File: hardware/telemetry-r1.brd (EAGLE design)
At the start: 63.5 x 63.5 mm, 113 parts, among them IC1 COPERNICUSSMD, IC10 TPS70933, IC2 TPS70933, IC3 74HC137, IC4 STM32L073CZT6, IC5 TPS62160, IC6 HX1, IC7 LMP7702, IC8 ADXL345, IC9 HIH9131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

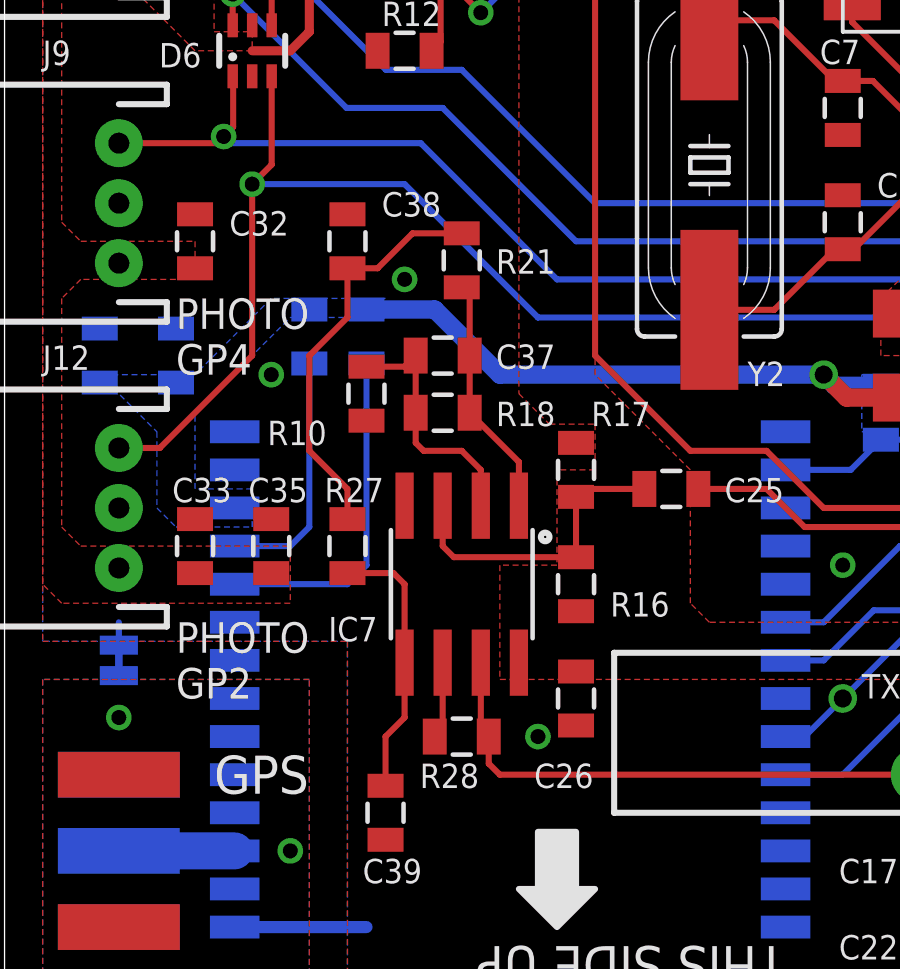
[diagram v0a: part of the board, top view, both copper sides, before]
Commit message: Update HX1 filter to match latest experimental results
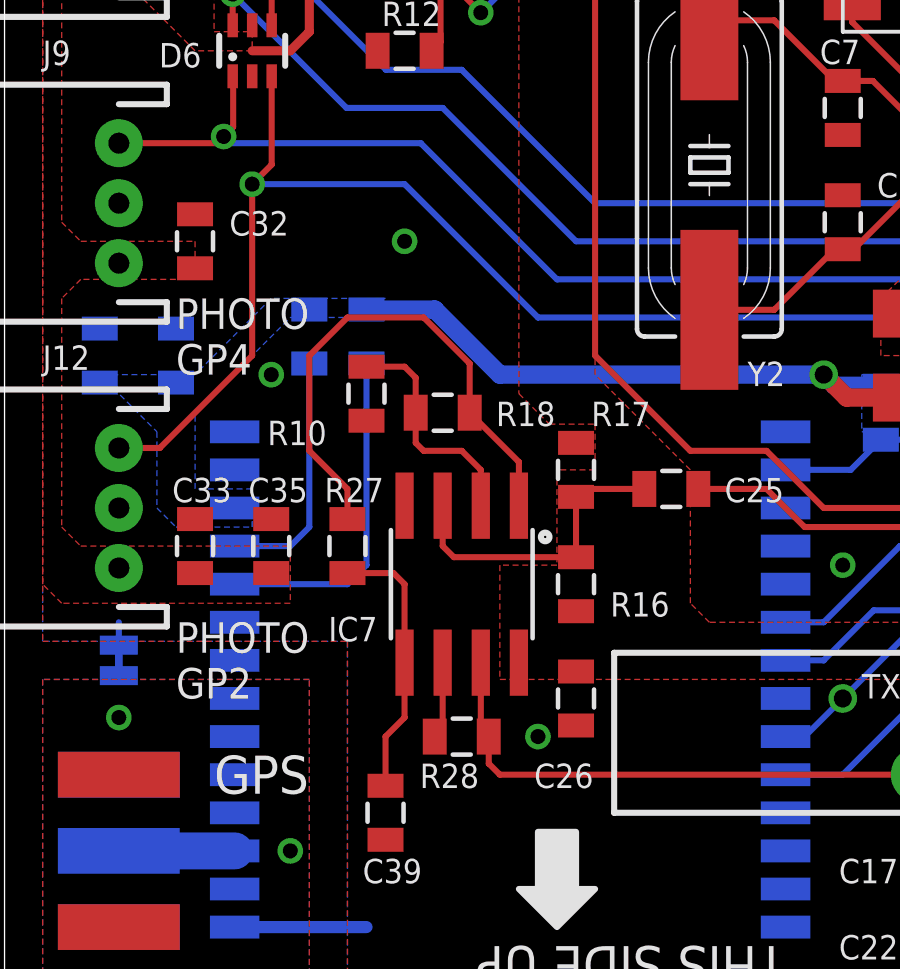
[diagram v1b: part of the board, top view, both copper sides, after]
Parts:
- removed C37: 100p, SparkFun-Passives:0805
- removed C38: 47n, SparkFun-Passives:0805
- removed R21: 680, SparkFun-Passives:0805
- R10: value 18K -> 470K
- R16: value 470K -> 820K
- R18: value 10K -> 680K
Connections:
- removed net LP3: C39.1, IC7.5, R27.2
- net A-: no longer C37.2
- net GND: no longer C38.2
- net LP1: now also R27.1; no longer C37.1, R21.1
- net LP2: now also C39.1, IC7.5, R27.2; no longer C38.1, R21.2, R27.1
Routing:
- net LP1: track 8.07 -> 17.9 mm
- net LP3: track 9.04 -> 0.00 mm
- net LP2: track 13.7 -> 9.04 mm
- net A-: track 8.44 -> 7.70 mm
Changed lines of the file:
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@@
 <attribute name="VALUE" x="40.513" y="15.621" size="0.6096" layer="27" rot="R270"/>
 </element>
-<element name="R16" library="SparkFun-Passives" package="0805" value="470K" x="19.05" y="15.24" smashed="yes" rot="R270">
+<element name="R16" library="SparkFun-Passives" package="0805" value="820K" x="19.05" y="15.24" smashed="yes" rot="R270">
 <attribute name="NAME" x="20.193" y="14.1605" size="0.8128" layer="25"/>
 <attribute name="VALUE" x="20.574" y="13.208" size="0.6096" layer="27"/>
@@
 <attribute name="VALUE" x="19.558" y="20.066" size="0.6096" layer="27" rot="R270"/>
 </element>
-<element name="R18" library="SparkFun-Passives" package="0805" value="10K" x="14.605" y="20.955" smashed="yes">
+<element name="R18" library="SparkFun-Passives" package="0805" value="680K" x="14.605" y="20.955" smashed="yes">
 <attribute name="NAME" x="16.383" y="20.5105" size="0.8128" layer="25"/>
 <attribute name="VALUE" x="16.764" y="21.463" size="0.6096" layer="27"/>
@@
 <element name="U$2" library="HAB" package="GARAGE" value="" x="29.21" y="41.91" rot="MR0"/>
 <element name="U$5" library="HAB" package="SWIFT" value="" x="27.305" y="52.705" rot="MR0"/>
-<element name="C37" library="SparkFun-Passives" package="0805" value="100p" x="14.605" y="22.86" smashed="yes" rot="R180">
-<attribute name="NAME" x="16.383" y="22.4155" size="0.8128" layer="25"/>
-<attribute name="VALUE" x="16.764" y="23.368" size="0.6096" layer="27"/>
-</element>
-<element name="R10" library="SparkFun-Passives" package="0805" value="18K" x="12.065" y="21.59" smashed="yes" rot="R90">
+<element name="R10" library="SparkFun-Passives" package="0805" value="470K" x="12.065" y="21.59" smashed="yes" rot="R90">
 <attribute name="NAME" x="8.763" y="19.8755" size="0.8128" layer="25"/>
 <attribute name="VALUE" x="9.779" y="20.828" size="0.6096" layer="27"/>
-</element>
-<element name="R21" library="SparkFun-Passives" package="0805" value="680" x="15.24" y="26.035" smashed="yes" rot="R90">
-<attribute name="NAME" x="16.383" y="25.5905" size="0.8128" layer="25"/>
-<attribute name="VALUE" x="16.129" y="26.543" size="0.6096" layer="27"/>
-</element>
-<element name="C38" library="SparkFun-Passives" package="0805" value="47n" x="11.43" y="26.67" smashed="yes" rot="R90">
-<attribute name="NAME" x="12.573" y="27.4955" size="0.8128" layer="25"/>
-<attribute name="VALUE" x="10.414" y="28.448" size="0.6096" layer="27"/>
 </element>
 <element name="R27" library="SparkFun-Passives" package="0805" value="330k" x="11.43" y="16.51" smashed="yes" rot="R270">
@@
 <contactref element="D10" pad="A"/>
 <contactref element="D4" pad="A"/>
-<contactref element="C38" pad="2"/>
 <contactref element="C39" pad="2"/>
 <contactref element="R10" pad="1"/>
 <contactref element="IC7" pad="4"/>
-<via x="13.335" y="25.4" extent="1-16" drill="0.5"/>
+<via x="13.335" y="26.67" extent="1-16" drill="0.5"/>
 </signal>
 <signal name="3.3V">
@@
 <signal name="A-">
 <contactref element="R10" pad="2"/>
-<contactref element="C37" pad="2"/>
 <contactref element="R18" pad="1"/>
-<wire x1="13.705" y1="20.955" x2="13.705" y2="22.86" width="0.2032" layer="1"/>
 <wire x1="12.065" y1="22.49" x2="13.335" y2="22.49" width="0.2032" layer="1"/>
-<wire x1="13.335" y1="22.49" x2="13.705" y2="22.86" width="0.2032" layer="1"/>
 <contactref element="IC7" pad="2"/>
 <wire x1="15.875" y1="17.8562" x2="15.875" y2="19.05" width="0.2032" layer="1"/>
@@
 <wire x1="13.705" y1="20.955" x2="13.705" y2="19.95" width="0.2032" layer="1"/>
 <wire x1="13.705" y1="19.95" x2="13.97" y2="19.685" width="0.2032" layer="1"/>
+<wire x1="13.705" y1="20.955" x2="13.705" y2="22.12" width="0.2032" layer="1"/>
+<wire x1="13.705" y1="22.12" x2="13.335" y2="22.49" width="0.2032" layer="1"/>
 </signal>
 <signal name="A+">
@@
 </signal>
 <signal name="LP1">
-<contactref element="R21" pad="1"/>
 <contactref element="IC7" pad="1"/>
 <contactref element="R18" pad="2"/>
-<contactref element="C37" pad="1"/>
 <wire x1="17.145" y1="17.8562" x2="17.145" y2="19.315" width="0.2032" layer="1"/>
 <wire x1="17.145" y1="19.315" x2="15.505" y2="20.955" width="0.2032" layer="1"/>
-<wire x1="15.505" y1="20.955" x2="15.505" y2="22.86" width="0.2032" layer="1"/>
-<wire x1="15.505" y1="22.86" x2="15.505" y2="24.87" width="0.2032" layer="1"/>
-<wire x1="15.505" y1="24.87" x2="15.24" y2="25.135" width="0.2032" layer="1"/>
-</signal>
-<signal name="LP2">
-<contactref element="C38" pad="1"/>
-<contactref element="R21" pad="2"/>
 <contactref element="R27" pad="1"/>
-<wire x1="11.43" y1="25.77" x2="12.435" y2="25.77" width="0.2032" layer="1"/>
-<wire x1="15.24" y1="26.935" x2="13.6" y2="26.935" width="0.2032" layer="1"/>
-<wire x1="13.6" y1="26.935" x2="12.435" y2="25.77" width="0.2032" layer="1"/>
 <wire x1="11.43" y1="17.41" x2="11.43" y2="18.415" width="0.2032" layer="1"/>
 <wire x1="11.43" y1="18.415" x2="10.16" y2="19.685" width="0.2032" layer="1"/>
 <wire x1="10.16" y1="19.685" x2="10.16" y2="22.86" width="0.2032" layer="1"/>
 <wire x1="10.16" y1="22.86" x2="11.43" y2="24.13" width="0.2032" layer="1"/>
-<wire x1="11.43" y1="25.77" x2="11.43" y2="24.13" width="0.2032" layer="1"/>
-</signal>
-<signal name="LP3">
-<contactref element="R27" pad="2"/>
-<contactref element="C39" pad="1"/>
+<wire x1="15.505" y1="20.955" x2="15.505" y2="22.595" width="0.2032" layer="1"/>
+<wire x1="15.505" y1="22.595" x2="13.97" y2="24.13" width="0.2032" layer="1"/>
+<wire x1="13.97" y1="24.13" x2="11.43" y2="24.13" width="0.2032" layer="1"/>
+</signal>
+<signal name="LP2">
 <contactref element="IC7" pad="5"/>
 <wire x1="13.335" y1="12.6238" x2="13.335" y2="10.795" width="0.2032" layer="1"/>
 <wire x1="13.335" y1="10.795" x2="12.7" y2="10.16" width="0.2032" layer="1"/>
-<wire x1="12.7" y1="10.16" x2="12.7" y2="8.52" width="0.2032" layer="1"/>
-<wire x1="11.43" y1="15.61" x2="12.965" y2="15.61" width="0.2032" layer="1"/>
 <wire x1="12.965" y1="15.61" x2="13.335" y2="15.24" width="0.2032" layer="1"/>
 <wire x1="13.335" y1="15.24" x2="13.335" y2="12.6238" width="0.2032" layer="1"/>
+<contactref element="R27" pad="2"/>
+<contactref element="C39" pad="1"/>
+<wire x1="12.965" y1="15.61" x2="11.43" y2="15.61" width="0.2032" layer="1"/>
+<wire x1="12.7" y1="8.52" x2="12.7" y2="10.16" width="0.2032" layer="1"/>
 </signal>
 <signal name="LP-">

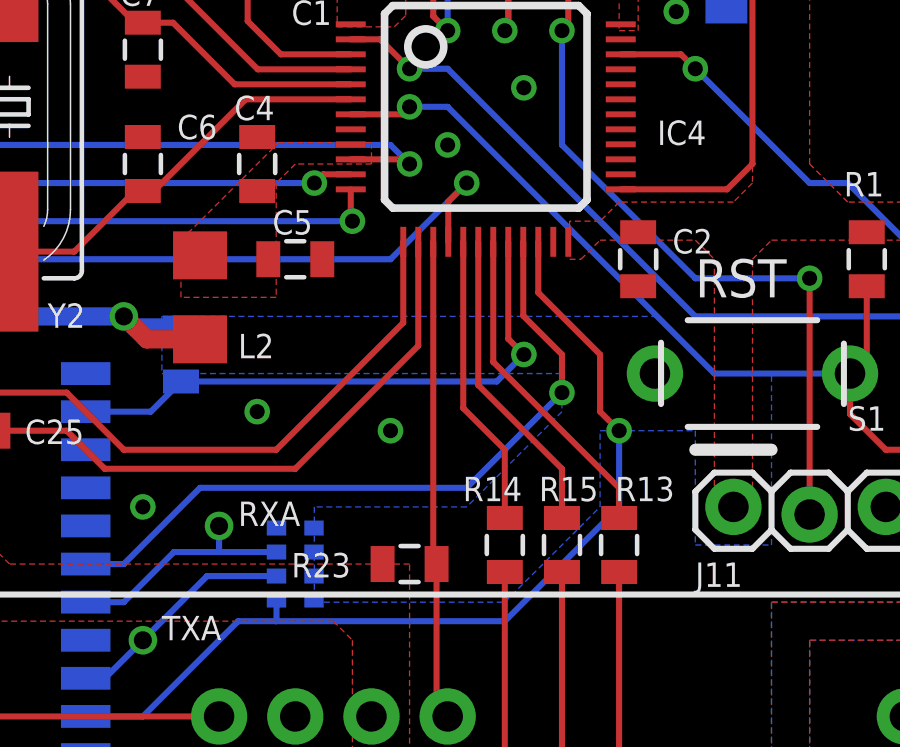
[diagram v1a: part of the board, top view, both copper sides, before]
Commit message: Swap HXEN pin to 5VT pin
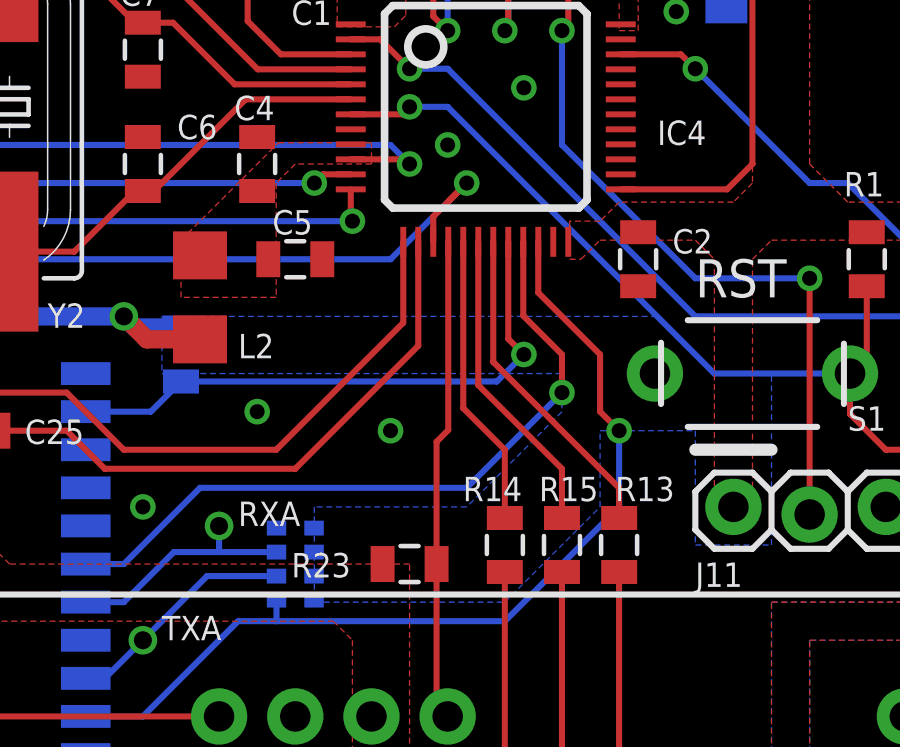
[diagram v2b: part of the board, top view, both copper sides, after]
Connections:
- net HXEN: now also IC4.16; no longer IC4.15
- net PHOTO_GP2: now also IC4.15; no longer IC4.16
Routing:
- net PHOTO_GP2: track 50.9 -> 52.0 mm
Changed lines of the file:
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@@
 <contactref element="IC6" pad="4"/>
 <contactref element="R23" pad="1"/>
-<contactref element="IC4" pad="15"/>
 <wire x1="37.73" y1="13.97" x2="37.73" y2="9.26" width="0.2032" layer="1"/>
 <wire x1="37.73" y1="9.26" x2="38.1" y2="8.89" width="0.2032" layer="1"/>
-<wire x1="37.62" y1="24.71" x2="37.62" y2="14.08" width="0.2032" layer="1"/>
 <wire x1="37.62" y1="14.08" x2="37.73" y2="13.97" width="0.2032" layer="1"/>
+<contactref element="IC4" pad="16"/>
+<wire x1="38.12" y1="24.71" x2="38.12" y2="18.435" width="0.2032" layer="1"/>
+<wire x1="37.73" y1="13.97" x2="37.73" y2="18.045" width="0.2032" layer="1"/>
+<wire x1="37.73" y1="18.045" x2="38.12" y2="18.435" width="0.2032" layer="1"/>
 </signal>
 <signal name="ADXL_SDO">
@@
 <contactref element="J12" pad="3"/>
 <contactref element="D6" pad="3"/>
-<contactref element="IC4" pad="16"/>
 <wire x1="8.905" y1="32.17" x2="8.905" y2="29.225" width="0.2032" layer="1"/>
 <wire x1="8.905" y1="29.225" x2="8.255" y2="28.575" width="0.2032" layer="1"/>
@@
 <wire x1="13.335" y1="28.575" x2="8.255" y2="28.575" width="0.2032" layer="16"/>
 <via x="8.255" y="28.575" extent="1-16" drill="0.5"/>
-<wire x1="38.12" y1="24.71" x2="38.12" y2="26.055" width="0.2032" layer="1"/>
 <wire x1="38.12" y1="26.055" x2="38.735" y2="26.67" width="0.2032" layer="1"/>
+<contactref element="IC4" pad="15"/>
+<wire x1="37.62" y1="24.71" x2="37.62" y2="25.555" width="0.2032" layer="1"/>
+<wire x1="37.62" y1="25.555" x2="38.735" y2="26.67" width="0.2032" layer="1"/>
 </signal>
 <signal name="USIN">

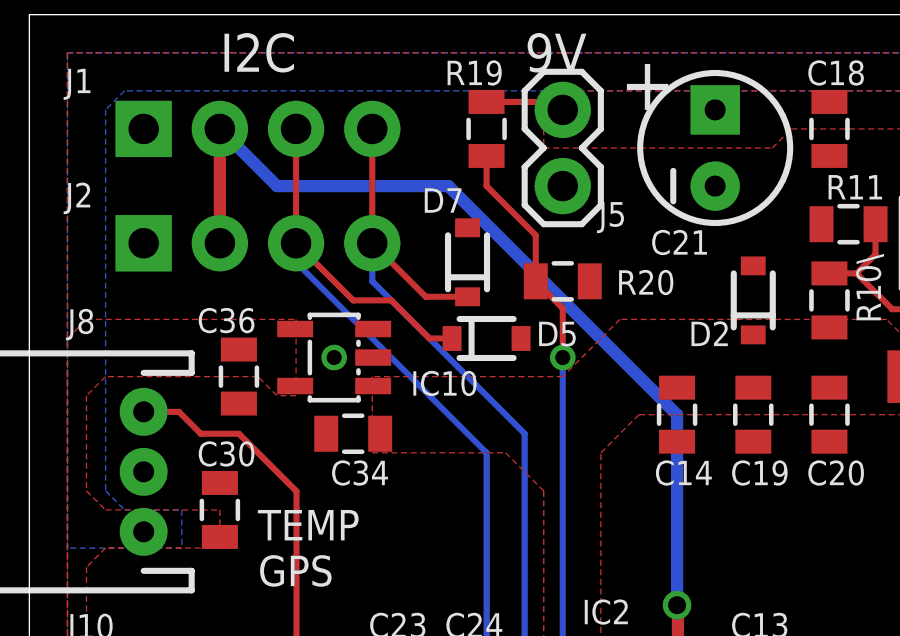
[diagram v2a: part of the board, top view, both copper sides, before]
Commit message: Fix I2C pull-up resistors in beta/regular boards; add Phoenix board and some datasheets
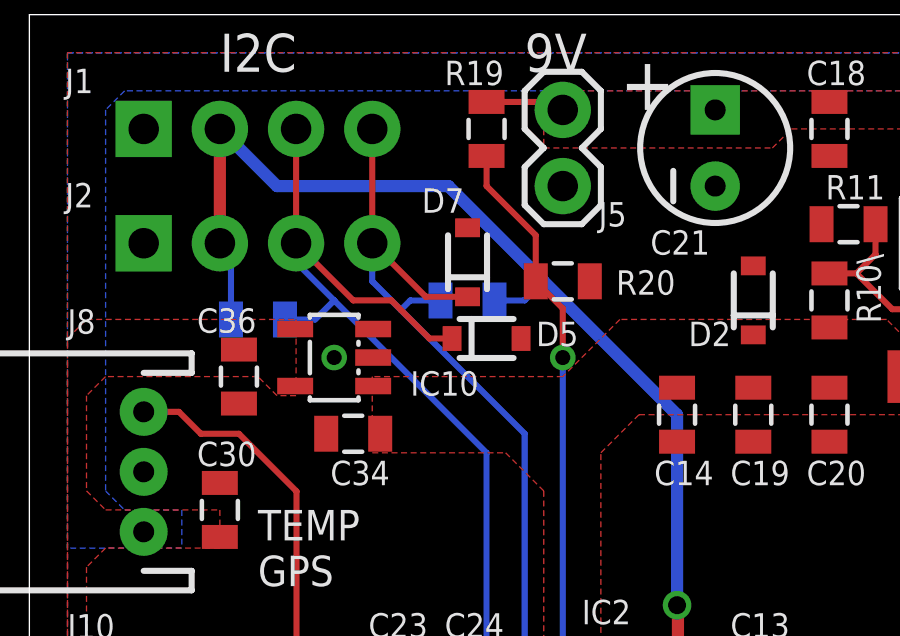
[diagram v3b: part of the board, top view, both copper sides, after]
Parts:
- added R21, R29: 4.7K, SparkFun-Passives:0805
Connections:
- net 3.3V: now also R21.1, R29.1
- net SCL: now also R21.2
- net SDA: now also R29.2
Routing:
- net 3.3V: track 86.8 -> 91.4 mm
- net SDA: track 63.2 -> 65.1 mm
- net SCL: track 54.3 -> 55.7 mm
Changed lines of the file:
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@@
 <attribute name="VALUE" x="14.859" y="7.493" size="0.6096" layer="27"/>
+</element>
+<element name="R21" library="SparkFun-Passives" package="0805" value="4.7K" x="14.605" y="53.975" smashed="yes" rot="MR0">
+<attribute name="NAME" x="15.367" y="54.8005" size="0.6096" layer="26" rot="MR0"/>
+<attribute name="VALUE" x="15.621" y="52.578" size="0.4064" layer="28" rot="MR0"/>
+</element>
+<element name="R29" library="SparkFun-Passives" package="0805" value="4.7K" x="7.62" y="53.34" smashed="yes" rot="MR180">
+<attribute name="NAME" x="6.858" y="52.5145" size="0.6096" layer="26" rot="MR180"/>
+<attribute name="VALUE" x="6.604" y="54.737" size="0.4064" layer="28" rot="MR180"/>
 </element>
 </elements>
@@
 <via x="21.59" y="43.815" extent="1-16" drill="0.6"/>
 <wire x1="21.59" y1="43.815" x2="21.59" y2="50.165" width="0.4064" layer="16"/>
-<wire x1="21.59" y1="50.165" x2="13.97" y2="57.785" width="0.4064" layer="16"/>
+<wire x1="21.59" y1="50.165" x2="17.145" y2="54.61" width="0.4064" layer="16"/>
+<wire x1="17.145" y1="54.61" x2="13.97" y2="57.785" width="0.4064" layer="16"/>
 <wire x1="13.97" y1="57.785" x2="8.255" y2="57.785" width="0.4064" layer="16"/>
 <wire x1="8.255" y1="57.785" x2="6.35" y2="59.69" width="0.4064" layer="16"/>
@@
 <vertex x="38.1" y="39.37"/>
 </polygon>
+<contactref element="R21" pad="1"/>
+<contactref element="R29" pad="1"/>
+<wire x1="15.505" y1="53.975" x2="16.51" y2="53.975" width="0.2032" layer="16"/>
+<wire x1="16.51" y1="53.975" x2="17.145" y2="54.61" width="0.2032" layer="16"/>
+<wire x1="6.72" y1="53.34" x2="6.72" y2="55.51" width="0.2032" layer="16"/>
+<wire x1="6.72" y1="55.51" x2="6.35" y2="55.88" width="0.2032" layer="16"/>
 </signal>
 <signal name="VDDA">
@@
 <wire x1="17.145" y1="36.83" x2="15.435" y2="36.83" width="0.2032" layer="1"/>
 <wire x1="11.43" y1="55.88" x2="11.43" y2="54.61" width="0.2032" layer="16"/>
-<wire x1="11.43" y1="54.61" x2="16.51" y2="49.53" width="0.2032" layer="16"/>
+<wire x1="11.43" y1="54.61" x2="12.3825" y2="53.6575" width="0.2032" layer="16"/>
+<wire x1="12.3825" y1="53.6575" x2="16.51" y2="49.53" width="0.2032" layer="16"/>
 <wire x1="16.51" y1="49.53" x2="16.51" y2="37.465" width="0.2032" layer="16"/>
 <wire x1="16.51" y1="37.465" x2="17.145" y2="36.83" width="0.2032" layer="16"/>
@@
 <wire x1="14.605" y1="54.095" x2="13.215" y2="54.095" width="0.2032" layer="1"/>
 <wire x1="13.215" y1="54.095" x2="11.43" y2="55.88" width="0.2032" layer="1"/>
+<contactref element="R21" pad="2"/>
+<wire x1="13.705" y1="53.975" x2="12.7" y2="53.975" width="0.2032" layer="16"/>
+<wire x1="12.7" y1="53.975" x2="12.3825" y2="53.6575" width="0.2032" layer="16"/>
 </signal>
 <signal name="SDA">
@@
 <wire x1="15.335" y1="34.83" x2="15.875" y2="34.29" width="0.2032" layer="1"/>
 <wire x1="8.89" y1="55.88" x2="8.89" y2="55.245" width="0.2032" layer="16"/>
-<wire x1="8.89" y1="55.245" x2="15.24" y2="48.895" width="0.2032" layer="16"/>
+<wire x1="8.89" y1="55.245" x2="10.16" y2="53.975" width="0.2032" layer="16"/>
+<wire x1="10.16" y1="53.975" x2="15.24" y2="48.895" width="0.2032" layer="16"/>
 <wire x1="15.24" y1="48.895" x2="15.24" y2="36.195" width="0.2032" layer="16"/>
 <wire x1="15.24" y1="36.195" x2="16.51" y2="34.925" width="0.2032" layer="16"/>
@@
 <wire x1="12.065" y1="53.975" x2="10.795" y2="53.975" width="0.2032" layer="1"/>
 <wire x1="10.795" y1="53.975" x2="8.89" y2="55.88" width="0.2032" layer="1"/>
+<contactref element="R29" pad="2"/>
+<wire x1="8.52" y1="53.34" x2="9.525" y2="53.34" width="0.2032" layer="16"/>
+<wire x1="9.525" y1="53.34" x2="10.16" y2="53.975" width="0.2032" layer="16"/>
 </signal>
 <signal name="CSA0">
